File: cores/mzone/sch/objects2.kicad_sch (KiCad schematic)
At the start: 16 parts

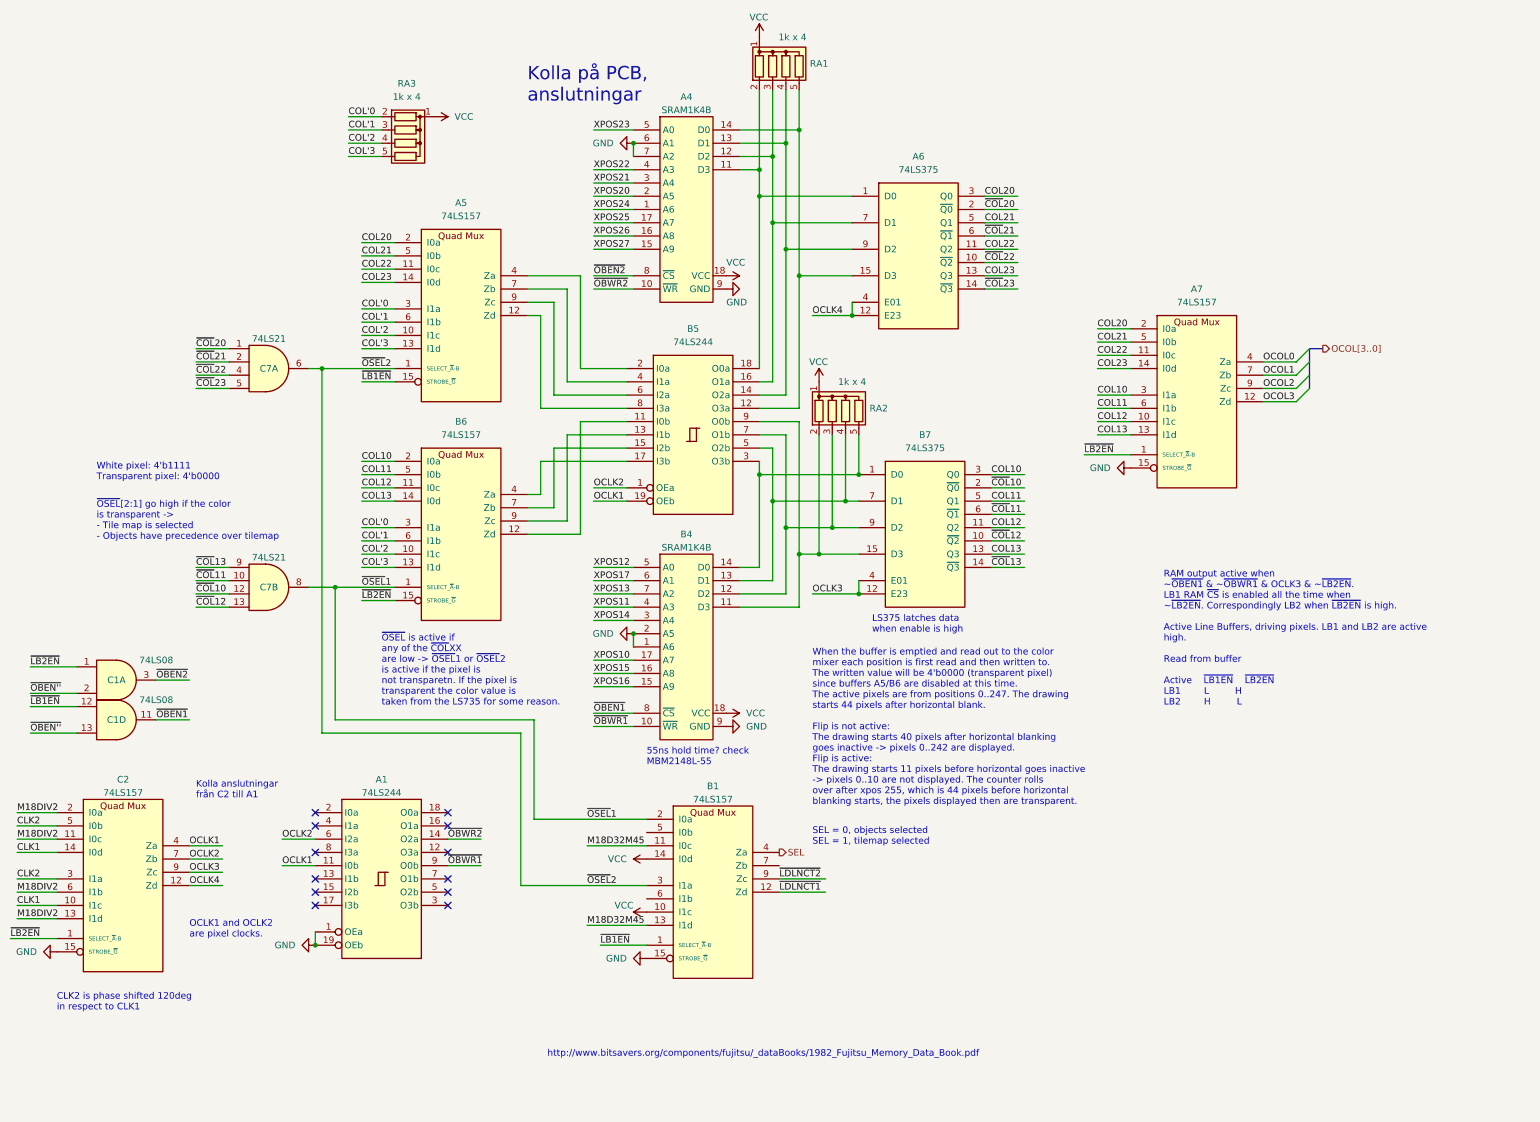
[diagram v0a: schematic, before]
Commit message: mzone core
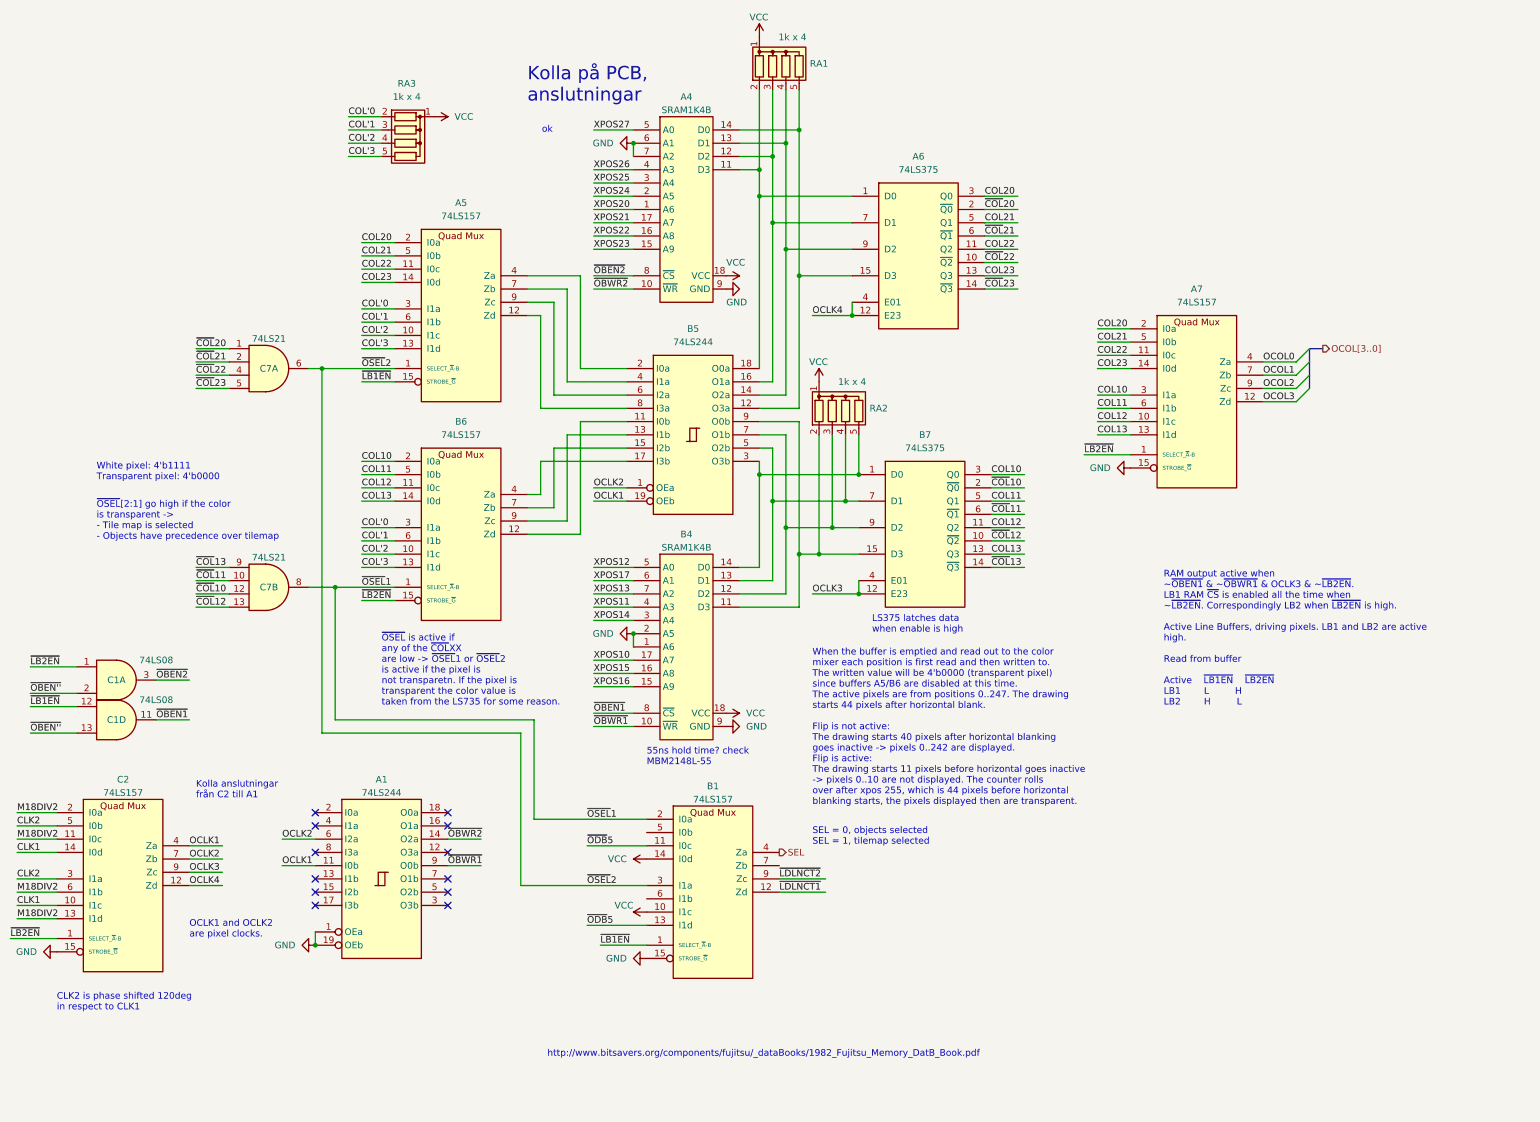
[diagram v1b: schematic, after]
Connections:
- net XPOS20: now also A4.1 (A6); no longer A4.2 (A5)
- net XPOS21: now also A4.17 (A7); no longer A4.3 (A4)
- net XPOS22: now also A4.16 (A8); no longer A4.4 (A3)
- net XPOS23: now also A4.15 (A9); no longer A4.5 (A0)
- net XPOS24: now also A4.2 (A5); no longer A4.1 (A6)
- net XPOS25: now also A4.3 (A4); no longer A4.17 (A7)
- net XPOS26: now also A4.4 (A3); no longer A4.16 (A8)
- net XPOS27: now also A4.5 (A0); no longer A4.15 (A9)
- net M18D32M45 renamed ~{ODB}5
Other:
- note added: "http://www.bitsavers.org/components/fujitsu/_dataBooks/1982_Fujitsu_Memory_DatB_Book.pdf"
- note added: "ok"
- note removed: "http://www.bitsavers.org/components/fujitsu/_dataBooks/1982_Fujitsu_Memory_Data_Book.pdf"

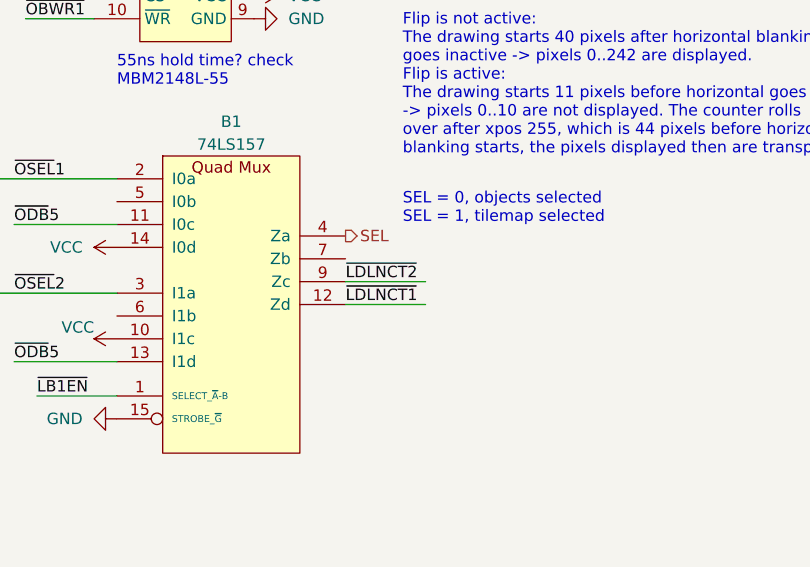
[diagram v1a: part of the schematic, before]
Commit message: mzone core
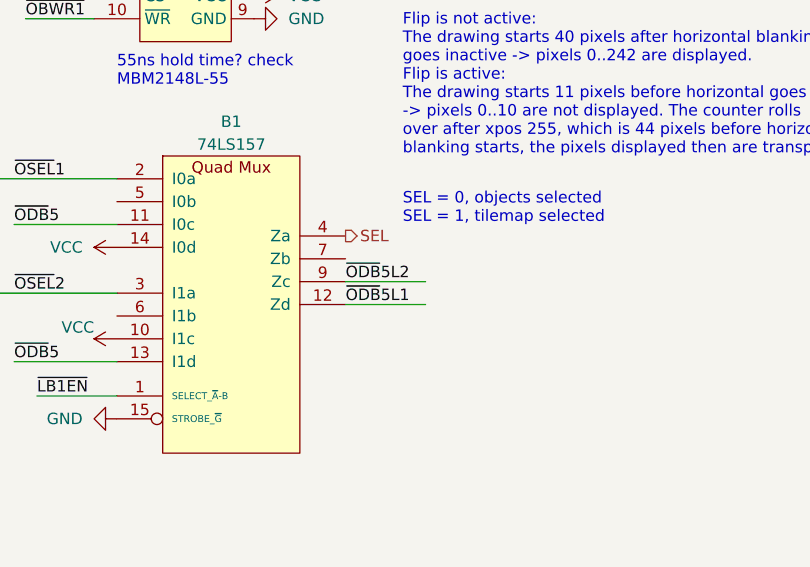
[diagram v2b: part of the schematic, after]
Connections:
- net ~{LDLNCT1} renamed ~{ODB}5L1
- net ~{LDLNCT2} renamed ~{ODB}5L2
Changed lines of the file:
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@@
 		)
 	)
-	(label "~{LDLNCT1}"
+	(label "~{ODB}5L1"
 		(at 274.32 213.36 0)
 		(fields_autoplaced yes)
@@
 		)
 	)
-	(label "~{LDLNCT2}"
+	(label "~{ODB}5L2"
 		(at 274.32 210.82 0)
 		(fields_autoplaced yes)

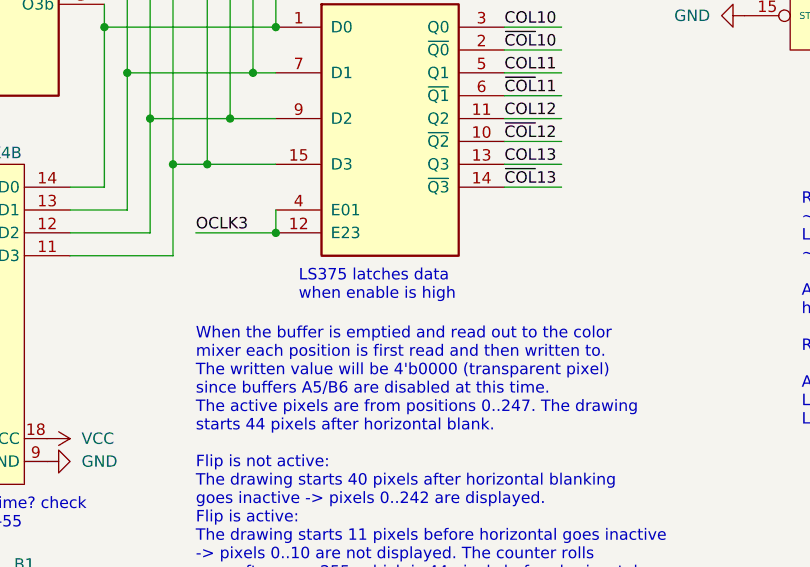
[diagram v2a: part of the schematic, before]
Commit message: mzone core
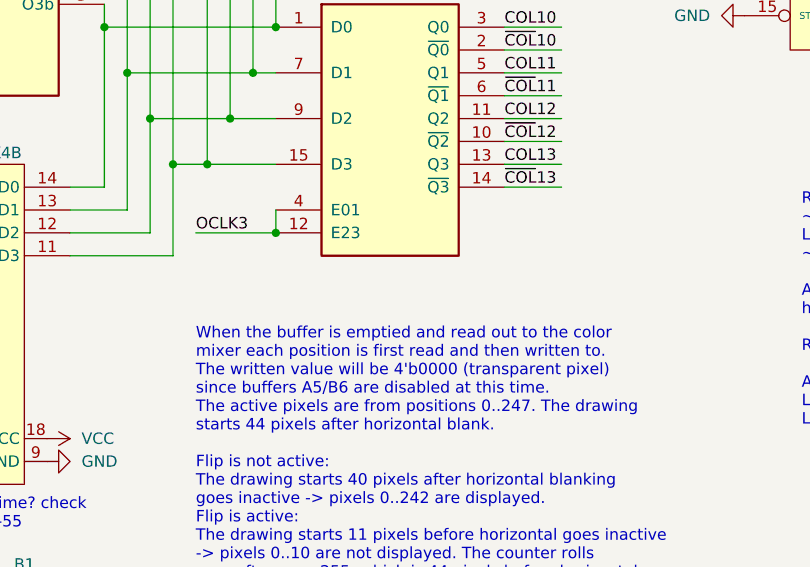
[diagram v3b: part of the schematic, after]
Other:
- note removed: "LS375 latches data when enable is high"
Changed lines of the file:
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@@
-		)
-	)
-	(text "LS375 latches data\nwhen enable is high"
-		(exclude_from_sim no)
-		(at 292.1 163.83 0)
-		(effects
-			(font
-				(size 1.27 1.27)
-			)
-			(justify left bottom)
 		)
 	)

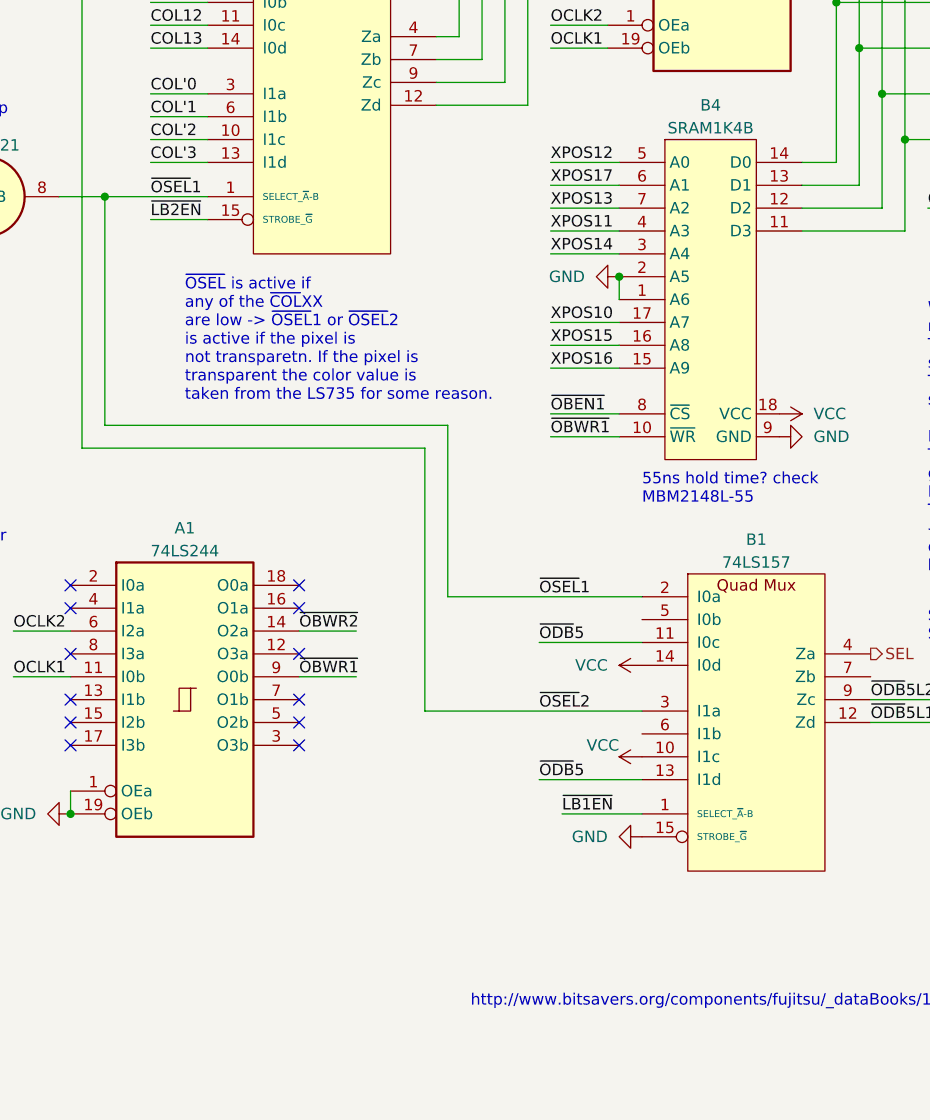
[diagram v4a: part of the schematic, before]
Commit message: mzone core
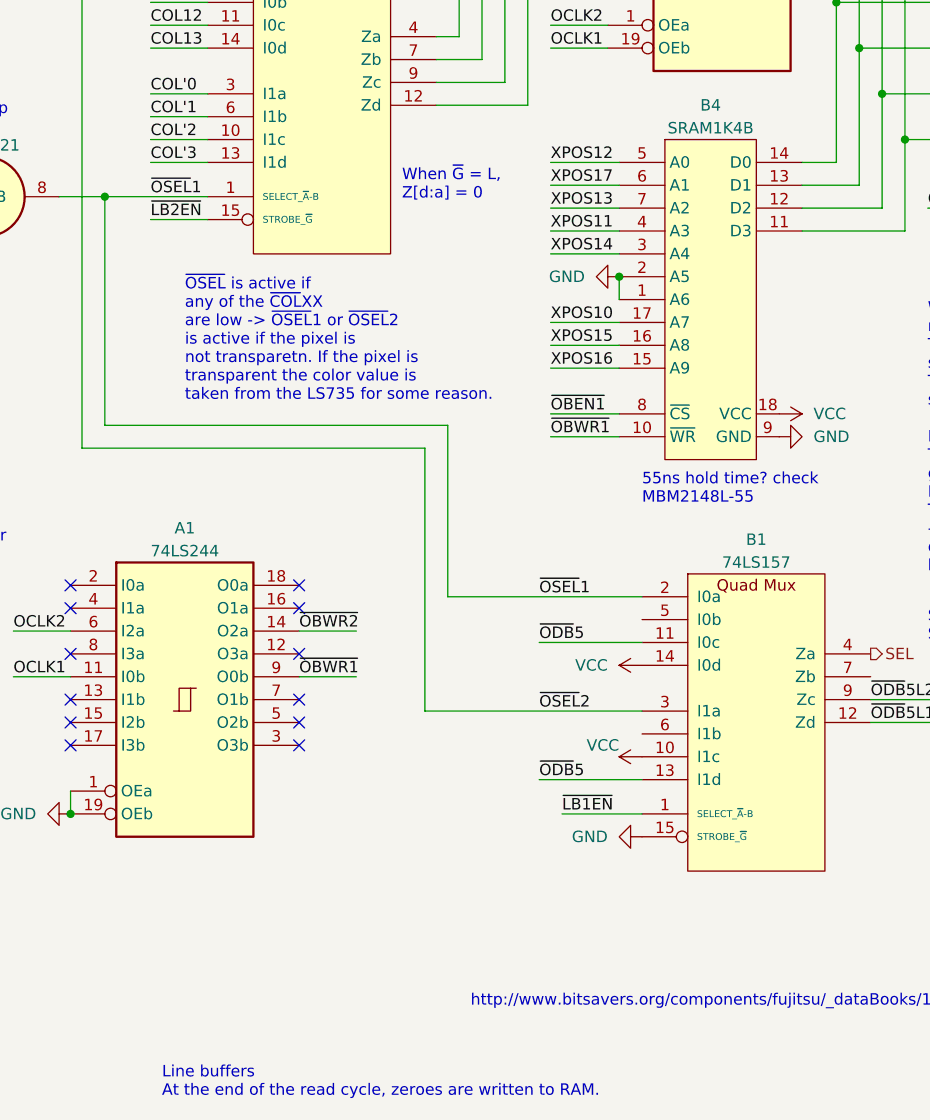
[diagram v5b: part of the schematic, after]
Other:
- note added: "Line buffers At the end of the read cycle, zeroes are written to RAM."
- note added: "When ~{G} = L, Z[d:a] = 0"
